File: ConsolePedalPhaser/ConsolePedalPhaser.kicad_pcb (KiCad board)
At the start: 2 copper layers, 100 x 60 mm, 56 parts, among them J1 Conn_02x25_Counter_Clockwise, Q1 2N5457, Q2 2N5457, Q3 2N5457, Q4 2N5457, Q5 2N3906, U1 TL072, U2 TL072, U3 TL072

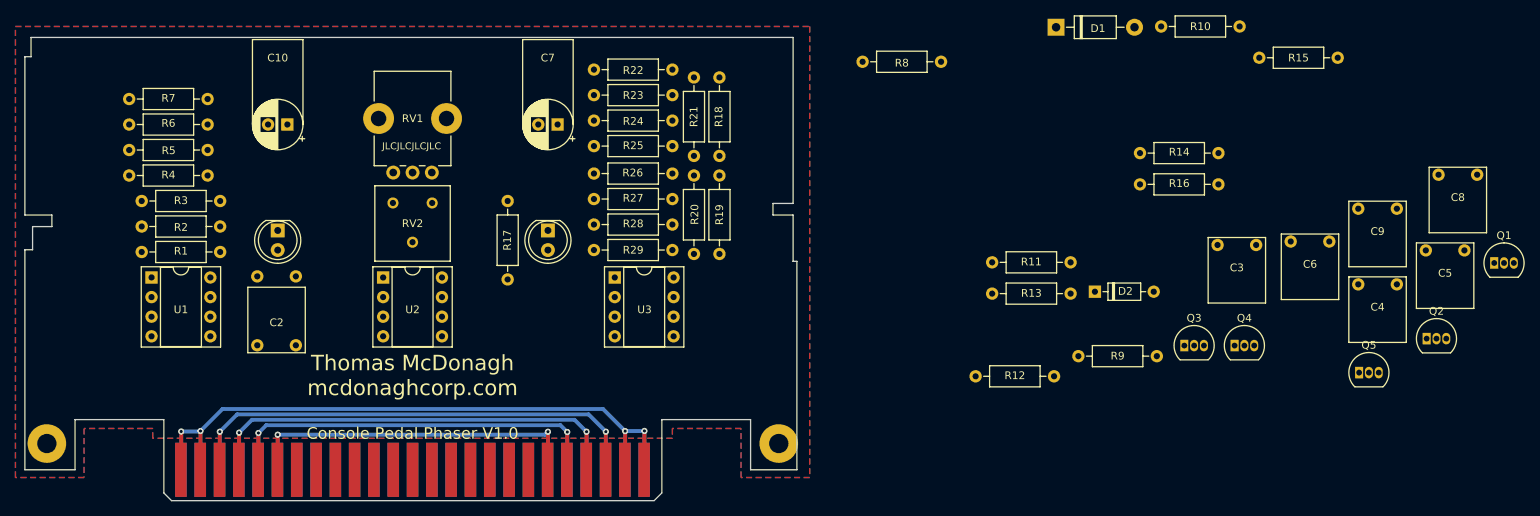
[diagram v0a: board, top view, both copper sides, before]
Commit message: Moved around some components
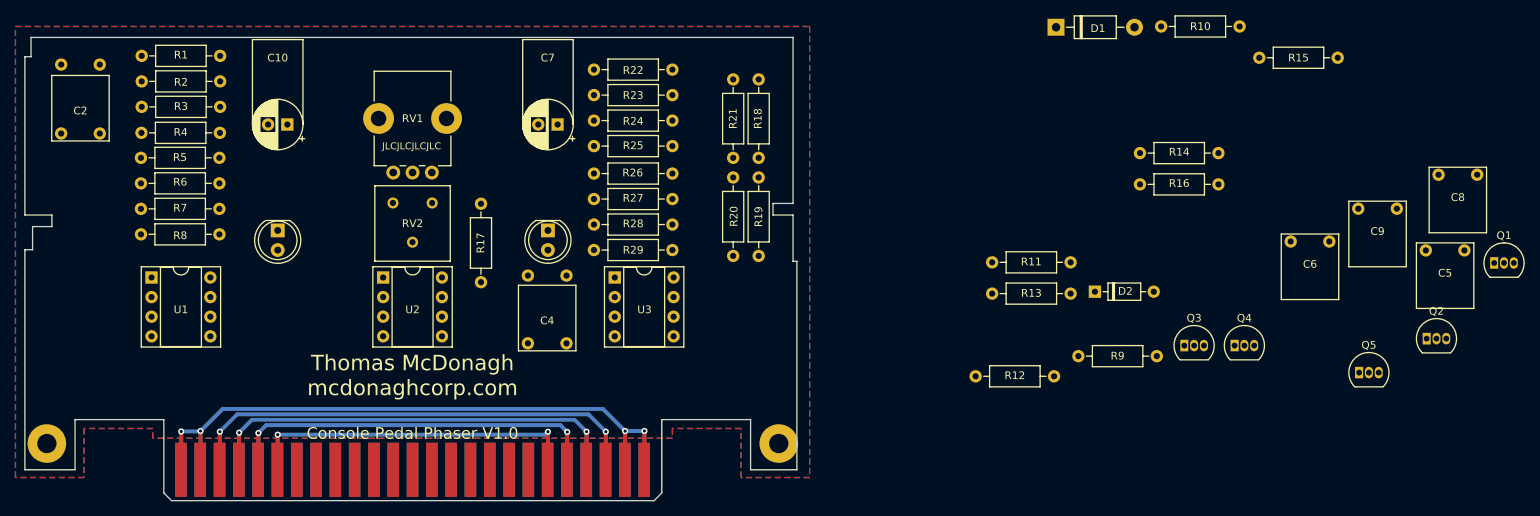
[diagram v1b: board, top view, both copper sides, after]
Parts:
- C3: moved to B.Cu
- moved C4 102.8 mm to (152.7, 109.2), turned to 180 degrees
- moved R8 96.1 mm to (97.5, 95.5)
- moved C3 84.4 mm to (152.7, 101.2), turned to 180 degrees
- moved C1 37.4 mm to (92.2, 73.9)
- moved C2 37.4 mm to (92.2, 82.0)
- moved R1 25.4 mm to (97.6, 72.4)
- moved R2 18.8 mm to (107.8, 75.7)
- moved R7 14.3 mm to (97.5, 92.2)
- moved R3 12.2 mm to (107.8, 79.0)
- moved R5 11.7 mm to (107.7, 85.6), turned to 180 degrees
- moved R6 7.77 mm to (97.5, 88.9)
- moved R4 5.75 mm to (97.6, 82.4)
- moved R20 5.09 mm to (174.2, 98.3)
- moved R21 5.09 mm to (174.2, 75.4)
- moved R18 5.09 mm to (177.5, 85.6)
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
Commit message: Finalized phaser board and made a quick board to test jfets for phaser circuit
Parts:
- C6, C9: moved to B.Cu
- moved Q1 153.3 mm to (121.2, 77.0)
- moved C5 146.8 mm to (117.6, 109.5), turned to 180 degrees
- moved R10 138.6 mm to (94.5, 99.3), turned to 90 degrees
- moved R14 135.2 mm to (94.5, 112.0), turned to 90 degrees
- moved Q5 133.6 mm to (121.9, 106.2)
- moved C6 128.9 mm to (117.6, 101.2), turned to 180 degrees
- moved Q2 126.2 mm to (142.0, 77.0)
- moved R12 117.1 mm to (91.2, 89.2), turned to 270 degrees
- moved R16 116.7 mm to (110.2, 90.4)
- moved R13 116.6 mm to (91.2, 101.9), turned to 270 degrees
- moved R9 112.0 mm to (107.7, 98.8), turned to 180 degrees
- moved Q3 111.6 mm to (121.9, 96.0)
- moved Q4 98.9 mm to (141.2, 96.0)
- moved D2 97.3 mm to (128.8, 72.1)
- moved R11 88.3 mm to (120.4, 86.6), turned to 180 degrees
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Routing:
- net +5V: track 0.00 -> 170.9 mm
- net Net-(R14-Pad2): track 0.00 -> 110.3 mm, vias 0 -> 1
- net Net-(C3-Pad1): track 0.00 -> 101.9 mm
- net +9V: track 60.1 -> 157.3 mm
- net Net-(C2-Pad1): track 0.00 -> 94.9 mm
- net /VBIAS: track 0.00 -> 94.8 mm
- net Net-(R10-Pad2): track 0.00 -> 87.2 mm
- net Net-(C5-Pad2): track 0.00 -> 87.1 mm
- net Net-(C9-Pad1): track 0.00 -> 86.9 mm
- net Net-(C9-Pad2): track 0.00 -> 86.8 mm
- net /Input: track 71.6 -> 156.6 mm
- net Net-(R13-Pad2): track 0.00 -> 80.5 mm
- net Net-(R25-Pad2): track 0.00 -> 79.7 mm
- net Net-(C3-Pad2): track 0.00 -> 75.4 mm
- net Net-(C4-Pad2): track 0.00 -> 74.8 mm
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- added copper zone on In1.Cu, net GND
- added copper zone on In2.Cu, net GND
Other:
- copper layers 2 -> 4
- board text added: "Thomas McDonagh consolepedals.com"
- board text removed: "Thomas McDonagh mcdonaghcorp.com"
